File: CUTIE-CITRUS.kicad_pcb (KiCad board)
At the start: 4 copper layers, 78.5 x 78.5 mm, 76 parts, among them J1 F32Q-1A7H1-11022, J2 F32Q-1A7H1-11022, J3 Bus_M.2_Socket_M, P1 ERM8-025-01-L-D-RA-K-TR, U1 AP3441SHE-7B, U2 ASEK-32.768KHZ-L-R-T, U3 ICM-42688-P, U5 MCP98243, U6 MCP98243, U7 MCP2518FD-xQBB, U8 TCAN334, Y1 ECS-2520MV-200-BN-TR

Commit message: power planes and sensor placement
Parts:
- removed TP1, TP2, TP3, TP4: TestPoint, TestPoint:TestPoint_Pad_D1.0mm
- 3V3, 5V0, GND1, GND2, GND4, GND5, TP10, TP11, TP12, TP13, TP14, TP15, TP17, TP18, TP19, TP20, TP21, TP5, TP6, TP9: moved to B.Cu
- moved U6 108.7 mm to (126.8, 76.2)
- moved C18 106.9 mm to (127.8, 74.3), turned to 180 degrees
- moved GND1 106.3 mm to (160.8, 73.8), turned to 180 degrees
- moved GND5 101.3 mm to (173.4, 119.2), turned to 180 degrees
- moved U5 99.0 mm to (122.2, 116.0)
- moved C15 96.3 mm to (121.6, 106.0), turned to 180 degrees
- moved Y1 96.0 mm to (121.6, 103.6), turned to 180 degrees
- moved U3 95.2 mm to (128.2, 110.8)
- moved C17 94.9 mm to (123.2, 114.0), turned to 180 degrees
- moved C14 94.6 mm to (126.5, 96.1)
- moved U7 94.6 mm to (125.5, 99.2)
- moved GND3 94.4 mm to (151.0, 86.8)
- moved R13 93.9 mm to (121.4, 99.2)
- moved U8 93.5 mm to (121.8, 90.0), turned to 90 degrees
- moved 5V0 93.4 mm to (128.2, 68.8), turned to 180 degrees
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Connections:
- net /Backplane Connector/CAN0.H renamed /Backplane Connector/CAN0.P
- net /Backplane Connector/CAN0.L renamed /Backplane Connector/CAN0.N
- CM5-1 pad 28: /CM5/I2C2.SDA -> /CM5/I2C2.SCL
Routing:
- net /CM5/CAM0_EN: track 0.00 -> 92.3 mm, vias 0 -> 1
- net /CM5/I2C0.SCL: track 0.00 -> 74.6 mm, vias 0 -> 1
- net /CM5/I2C0.SDA: track 0.00 -> 69.9 mm, vias 0 -> 1
- net /Backplane Connector/SPI2.MISO: track 0.00 -> 49.1 mm, vias 0 -> 1
- net /Backplane Connector/SPI2.CS0n: track 0.00 -> 48.2 mm, vias 0 -> 1
- net /Backplane Connector/CAN0.P: track 0.00 -> 45.6 mm
- net /Backplane Connector/CAN0.N: track 0.00 -> 45.4 mm
- net /CM5/CAM1_EN: track 0.00 -> 45.1 mm, vias 0 -> 1
- net /Backplane Connector/SPI2.SCLK: track 0.00 -> 42.9 mm, vias 0 -> 1
- net /Backplane Connector/SPI2.MOSI: track 0.00 -> 42.0 mm, vias 0 -> 1
- net /CM5/I2C1.SDA: track 0.00 -> 36.4 mm, vias 0 -> 1
- net /CM5/I2C1.SCL: track 0.00 -> 33.7 mm, vias 0 -> 1
- net /CM5/I2C2.SDA: track 0.00 -> 29.9 mm, vias 0 -> 1
- net /CM5/I2C2.SCL: track 0.00 -> 24.5 mm, vias 0 -> 1
- net GND: track 14.1 -> 35.5 mm, vias 59 -> 76
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- added copper zone on B.Cu, net /CM5/3V3
- added copper zone on F.Cu, net /CM5/3V3
- added copper zone on In1.Cu, net /CM5/3V3

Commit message: preliminary layout complete
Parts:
- removed TP15: TestPoint, TestPoint:TestPoint_Pad_D1.0mm
- 3V3, GND4, TP10, TP9: moved to F.Cu
- moved R10 44.7 mm to (127.5, 116.8), turned to 90 degrees
- moved R9 44.0 mm to (117.5, 115.8)
- moved GND3 32.5 mm to (178.5, 69.5)
- moved TP11 32.0 mm to (135.0, 110.0)
- moved D2 31.1 mm to (124.8, 133.0)
- moved TP10 30.6 mm to (133.4, 108.0), turned to 0 degrees
- moved TP13 29.6 mm to (129.5, 104.0)
- moved R4 29.5 mm to (124.8, 131.5)
- moved TP14 29.0 mm to (129.0, 96.0)
- moved TP12 28.5 mm to (127.5, 104.8)
- moved D1 25.1 mm to (120.5, 133.0)
- moved R3 23.8 mm to (120.5, 131.5)
- moved TP9 21.4 mm to (120.5, 111.3), turned to 0 degrees
- moved GND4 19.9 mm to (118.2, 128.2), turned to 0 degrees
- moved GND1 18.2 mm to (178.5, 69.5)
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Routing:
- net GND: track 35.5 -> 200.8 mm, vias 76 -> 190
- net /CM5/3V3: track 7.13 -> 77.4 mm, vias 10 -> 24
- net Net-(CM5-1A-LED_nPWR): track 0.00 -> 50.6 mm, vias 0 -> 2
- net /CM5/I2C2.SDA: track 29.9 -> 76.2 mm
- net Net-(CM5-1A-LED_nACT): track 0.00 -> 40.1 mm, vias 0 -> 2
- net /CM5/I2C2.SCL: track 24.5 -> 63.8 mm
- net /CM5/SPI1.MOSI: track 11.3 -> 16.3 mm
- net /CM5/I2C1.SCL: track 33.7 -> 38.5 mm, vias 1 -> 3
- net /CM5/SPI1.SCLK: track 10.3 -> 12.5 mm
- net Net-(D2-K): track 0.00 -> 1.61 mm
- net Net-(D1-K): track 0.00 -> 1.61 mm
- net /CM5/SPI1.CS0n: track 19.3 -> 20.9 mm
- net /CM5/SPI1.MISO: track 19.6 -> 20.9 mm
- net /CM5/CAM0_EN: track 92.3 -> 93.0 mm, vias 1 -> 3
- net /Backplane Connector/USB3.D_P: vias 0 -> 1
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
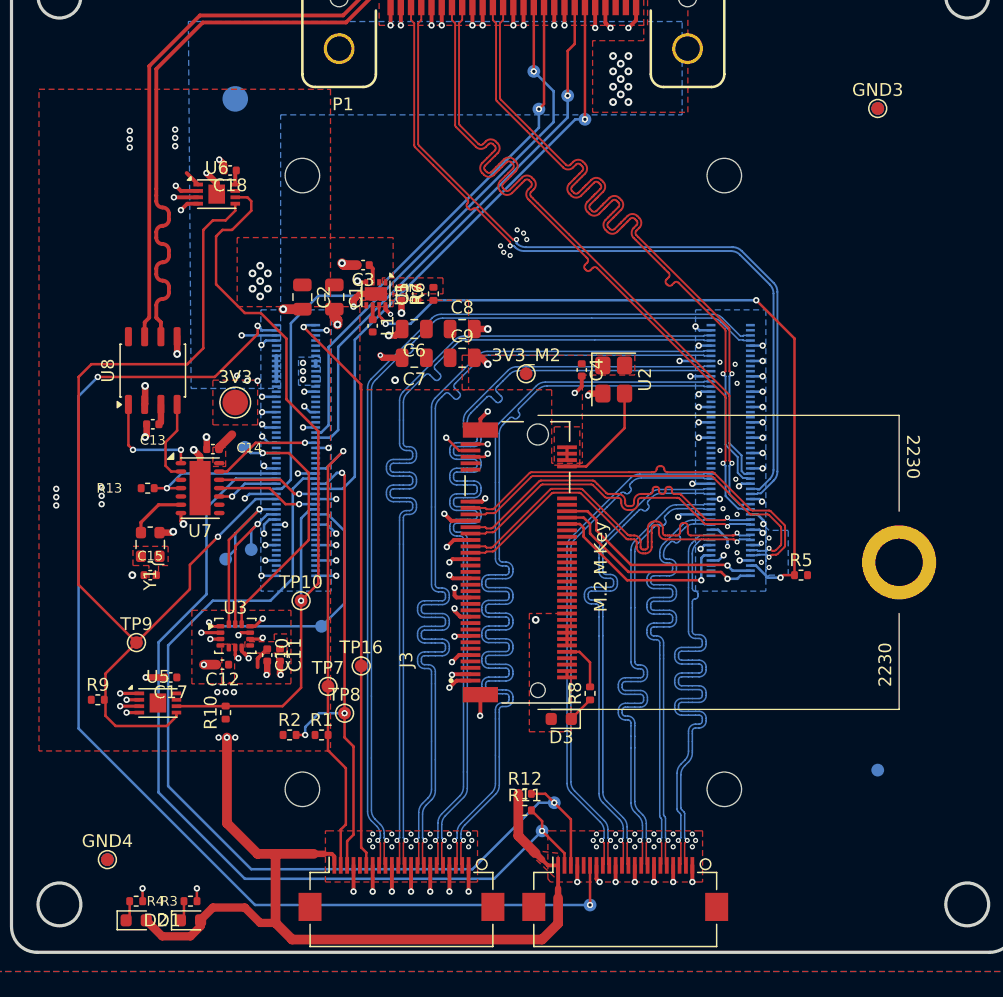
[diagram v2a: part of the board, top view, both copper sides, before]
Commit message: silkscreen edits
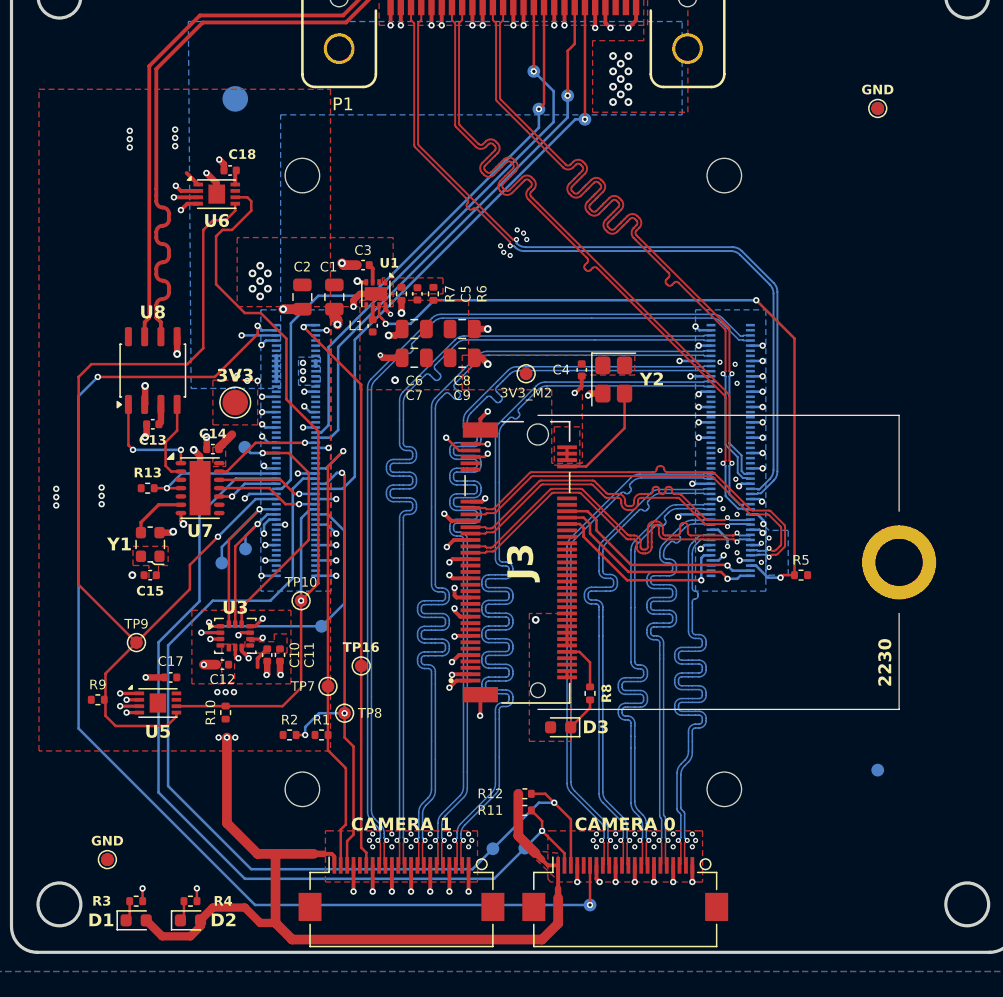
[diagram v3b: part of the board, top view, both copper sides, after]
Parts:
- moved TP6 6.00 mm to (148.4, 127.4)
- moved TP5 1.91 mm to (150.9, 127.3)
- moved D3 0.65 mm to (153.7, 117.9)
- moved TP13 0.45 mm to (129.1, 104.0)
- moved TP12 0.42 mm to (127.2, 105.0)
- renumbered CM5-1 to CM5, GND4 to GND, GND3 to GND, GND5 to GND, GND1 to GND, GND2 to GND, U2 to Y2
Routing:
- net Net-(D3-K): track 2.10 -> 2.77 mm
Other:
- board text added: "CAMERA 0"
- board text added: "CAMERA 1"

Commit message: drc fixes, verification
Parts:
- moved C15 0.18 mm to (121.7, 106.1)
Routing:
- net GND: track 200.8 -> 201.7 mm
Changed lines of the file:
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@@
 	(footprint "Capacitor_SMD:C_0402_1005Metric"
 		(layer "F.Cu")
-		(at 121.6 106 180)
+		(at 121.707836 106.14 180)
 		(descr "Capacitor SMD 0402 (1005 Metric), square (rectangular) end terminal, IPC-7351 nominal, (Body size source: IPC-SM-782 page 76, https://www.pcb-3d.com/wordpress/wp-content/uploads/ipc-sm-782a_amendment_1_and_2.pdf), generated with kicad-footprint-generator")
 		(tags "capacitor")
@@
 	)
 	(segment
-		(start 151.45 131.75)
-		(end 151.25 131.75)
-		(width 0.05)
-		(layer "F.Cu")
-		(net 0)
-	)
-	(segment
 		(start 128.25 74.43)
 		(end 128.33 74.35)
@@
 	)
 	(segment
+		(start 120.307836 106.14)
+		(end 121.227836 106.14)
+		(width 0.508)
+		(layer "F.Cu")
+		(net 4)
+	)
+	(segment
 		(start 146.648 96.25)
 		(end 145.75 96.25)
@@
 	)
 	(via
-		(at 120.2 106)
+		(at 120.307836 106.14)
 		(size 0.61)
 		(drill 0.3)
@@
 		(layer "F.Cu")
 		(hatch full 0.5)
-		(priority 8)
-		(connect_pads yes
-			(clearance 0.25)
-		)
-		(min_thickness 0.25)
-		(filled_areas_thickness no)
-		(fill yes
-			(thermal_gap 0.5)
-			(thermal_bridge_width 0.5)
-			(smoothing fillet)
-			(radius 0.2)
-		)
-		(polygon
-			(pts
-				(xy 120.25 103.75) (xy 123 103.75) (xy 123 105.25) (xy 122.25 105.25) (xy 122.25 106.25) (xy 121.5 106.25)
-				(xy 121.5 105.25) (xy 120.25 105.25)
-			)
-		)
-	)
-	(zone
-		(net 1)
-		(net_name "/CM5/3V3")
-		(layer "F.Cu")
-		(hatch full 0.5)
 		(priority 12)
 		(connect_pads yes
@@
 		(polygon
 			(pts
-				(xy 131.3 110.6) (xy 131.3 111.2) (xy 129 111.2) (xy 129 112.1) (xy 132.3 112.1) (xy 132.3 110.6)
+				(xy 131.3 111.2) (xy 131.3 111.2) (xy 129 111.2) (xy 129 112.1) (xy 131.5 112.1) (xy 131.5 111.2)
 			)
 		)
@@
 		(layer "F.Cu")
 		(hatch full 0.5)
-		(priority 1)
+		(priority 2)
 		(connect_pads yes
 			(clearance 0.5)
@@
 		(layer "B.Cu")
 		(hatch edge 0.5)
-		(priority 1)
+		(priority 2)
 		(connect_pads yes
 			(clearance 0.25)

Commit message: added missing 3d files, added slksc graphics
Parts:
- added G***: LOGO, library:hsp-logo, F.Cu at (180.0, 76.8)
- added G***: LOGO, library:hsp, F.Cu at (179.2, 77.0)
- added G***: LOGO, library:hsp-logo, B.Cu at (121.8, 84.8)
- added G***: LOGO, LOGO, B.Cu at (177.2, 72.2)
- added G***: LOGO, LOGO, B.Cu at (150.2, 87.2)
- added G***: LOGO, library:emoji-brainrot, B.Cu at (179.2, 120.8)
- added G***: LOGO, library:aibaby, B.Cu at (150.2, 102.0)
- added G***: LOGO, library:miffy2, B.Cu at (120.6, 122.3)
- added REF**: ESD-Logo_8.9x8mm_SilkScreen, Symbol:ESD-Logo_8.9x8mm_SilkScreen, F.Cu at (120.5, 66.8)
- added REF**: WEEE-Logo_5.6x8mm_SilkScreen, Symbol:WEEE-Logo_5.6x8mm_SilkScreen, F.Cu at (175.2, 130.2)
- moved GND 78.6 mm to (121.7, 66.9)
- moved GND 66.5 mm to (121.4, 103.6)
- moved GND 50.2 mm to (141.8, 103.8)
- moved GND 44.7 mm to (162.7, 132.7)
- moved GND 4.74 mm to (121.7, 125.0)
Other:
- board text added: "A"
- board text added: "Board"
- board text added: "CUTIE-CITRUS"
- board text added: "Revision"
- board text added: "SN"
- board text added: "designed by andre s winkel et al for highlander space program at ucr"

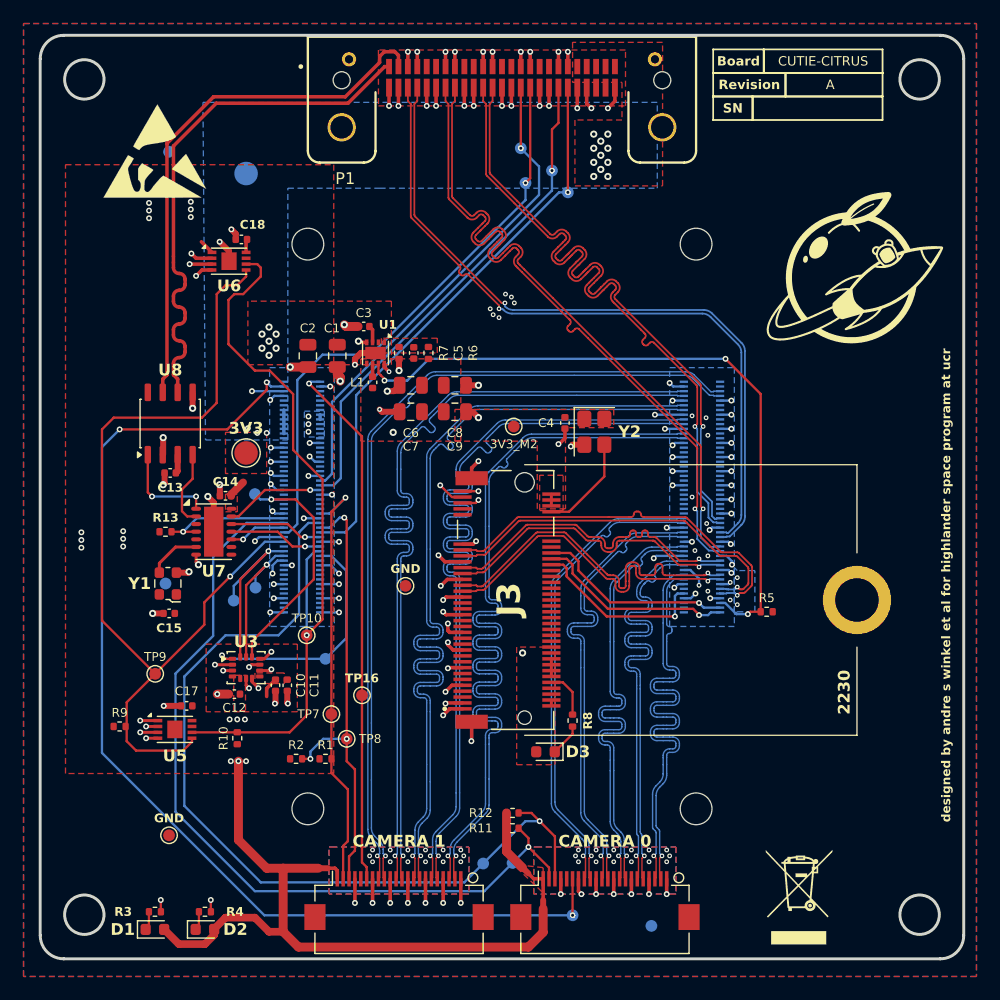
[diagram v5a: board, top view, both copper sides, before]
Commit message: silkscreen, via stitching
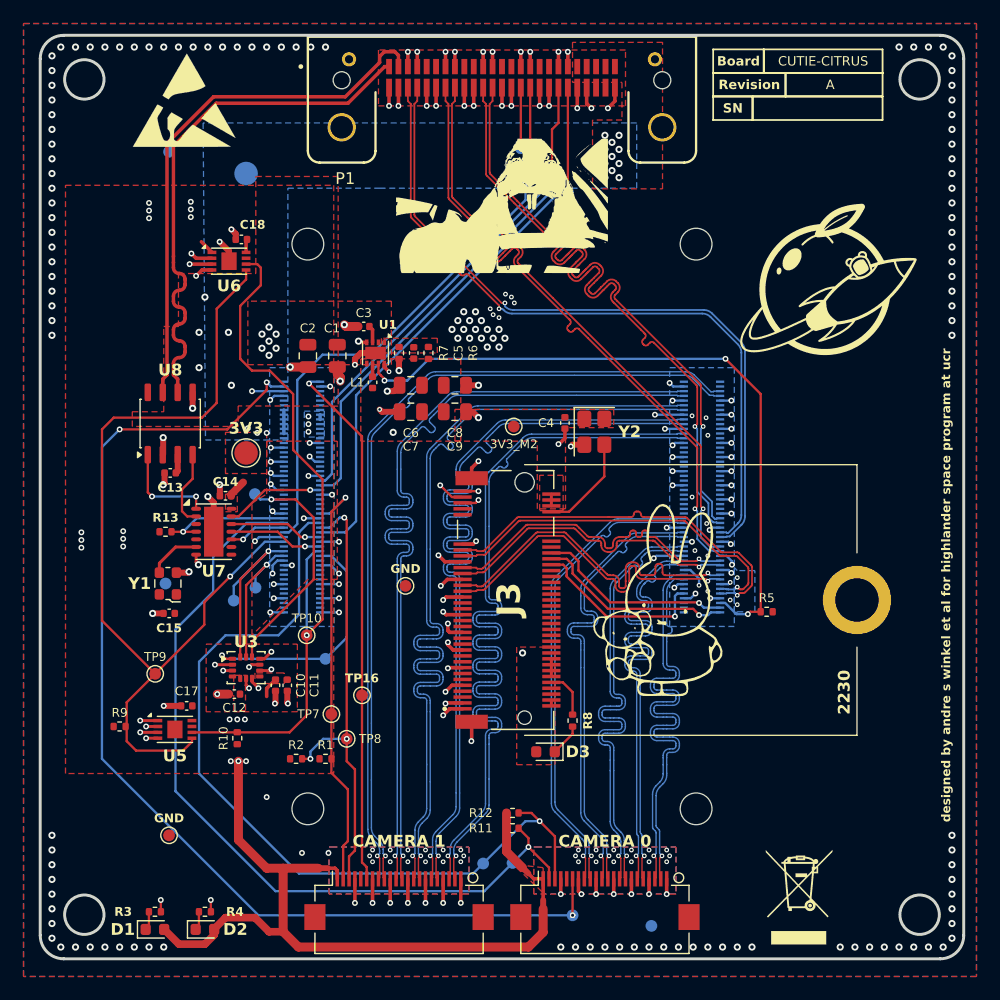
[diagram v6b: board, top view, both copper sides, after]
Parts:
- removed the G*** at (121.8, 84.8)
- removed the G*** at (179.2, 120.8)
- removed the G*** at (150.2, 102.0)
- added G***: LOGO, LOGO, B.Cu at (121.2, 79.0)
- added G***: LOGO, LOGO, B.Cu at (179.5, 93.5)
- added G***: LOGO, LOGO, B.Cu at (150.0, 101.2)
- added G***: LOGO, LOGO, B.Cu at (179.5, 118.8)
- G*** (x2): moved to F.Cu
- moved G*** 47.1 mm to (164.2, 104.4), turned to 0 degrees
- moved G*** 15.8 mm to (150.0, 71.5), turned to 0 degrees
- moved REF** 4.99 mm to (123.0, 62.5)
- moved G*** 2.46 mm to (177.8, 77.8)
- moved G*** 1.77 mm to (178.5, 73.5)
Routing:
- net /CM5/I2C0.SCL: track 74.6 -> 70.6 mm
- net Net-(CM5-1A-LED_nPWR): track 50.6 -> 49.2 mm
- net /CM5/I2C2.SCL: track 63.8 -> 62.7 mm
- net /CM5/I2C0.SDA: track 69.9 -> 68.9 mm
- net Net-(CM5-1A-LED_nACT): track 40.1 -> 41.0 mm
- net /CM5/I2C2.SDA: track 76.2 -> 75.6 mm
- net GND: vias 190 -> 324
